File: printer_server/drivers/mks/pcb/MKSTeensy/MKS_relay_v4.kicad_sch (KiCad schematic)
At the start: 66 parts, among them J1 Conn_01x03, J10 Conn_01x02, J11 Conn_01x02, J12 Conn_01x02, J13 Conn_01x02, J14 Conn_01x02, J15 Conn_01x02, J16 Conn_01x02, J17 Conn_01x02, J18 Conn_01x02, J19 Conn_01x02, J2 Conn_01x04, J20 Conn_01x02, J21 Conn_01x02, J22 DB25_Receptacle_MountingHoles, J3 Barrel_Jack_PTH, J4 Conn_01x02, J5 Conn_01x02, J6 Conn_01x02, J7 Conn_01x02, J8 Conn_01x02, J9 Conn_01x02, Q1 IRLZ34N, Q2 IRLZ34N, Q3 IRLZ34N, Q4 IRLZ34N, Q5 IRLZ34N, Q6 IRLZ34N, Q7 IRLZ34N, Q8 IRLZ34N, Q9 IRLZ34N, U1 Teensy4.0

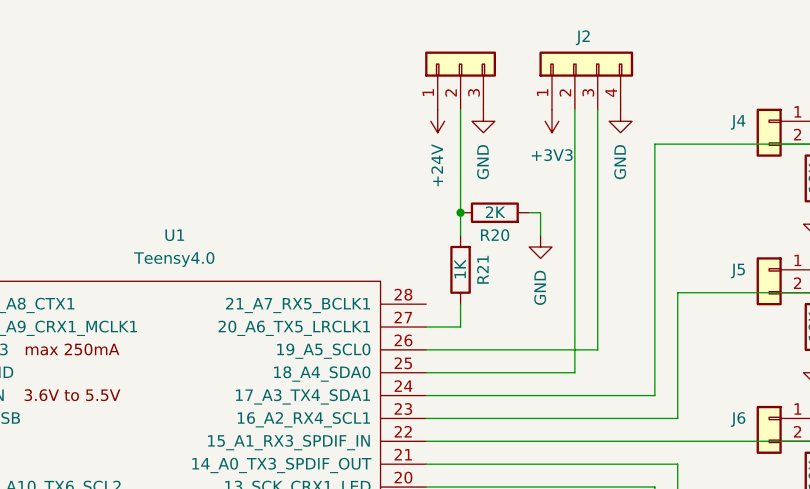
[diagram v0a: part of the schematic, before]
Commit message: Fix voltage divider in  MKS PCB
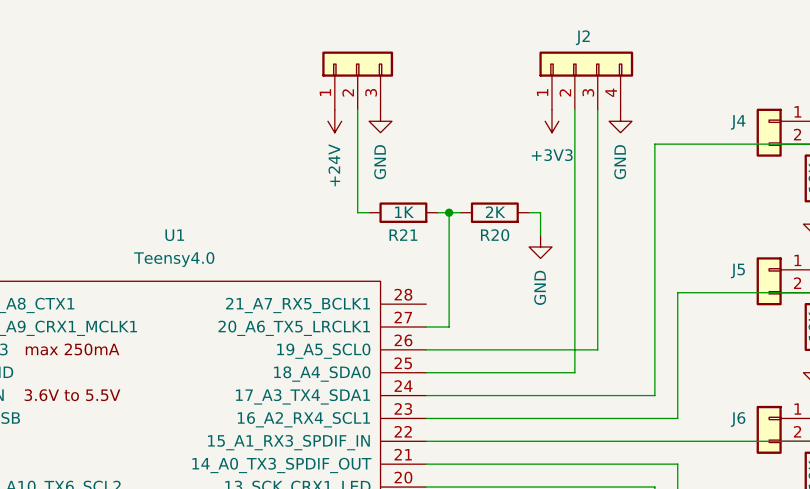
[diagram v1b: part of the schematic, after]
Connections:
- net at R20.1, R21.2: now also U1.27 (20_A6_TX5_LRCLK1); no longer J1.2 (Pin_2)
- net at R21.1: now also J1.2 (Pin_2); no longer U1.27 (20_A6_TX5_LRCLK1)
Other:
- moved on the sheet: R21
